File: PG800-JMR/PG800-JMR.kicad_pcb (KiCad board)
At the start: 2 copper layers, 93.5 x 124.5 mm, 51 parts, among them J1 DIN-6, J10 POT_POWER_2, J11 POT_POWER_3, J2 POT_CENTERS_1, J3 POT_CENTERS_2, J4 POT_CENTERS_3, J5 SWITCH_BLK, J6 TEENSY_PIN_BLK1, J7 TEENSY_PIN_BLK3, J8 TEENSY_PIN_BLK2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

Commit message: updated kicad drawings, tweaked code slightly
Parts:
- added J12: GND_BLK, Connector_PinHeader_2.54mm:PinHeader_1x09_P2.54mm_Vertical, F.Cu at (21.9, 112.5)
- added J13: 3.3V_BLK, Connector_PinHeader_2.54mm:PinHeader_1x09_P2.54mm_Vertical, F.Cu at (17.8, 86.5)
- added J14: 5V_BLK, Connector_PinHeader_2.54mm:PinHeader_1x09_P2.54mm_Vertical, F.Cu at (21.7, 86.5)
- moved C7 3.09 mm to (15.7, 120.0)
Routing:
- net +5V: track 107.8 -> 137.4 mm
- net Net-(U3-~{E}): track 133.8 -> 139.0 mm
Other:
- board text added: "JMR-800 JX8P Controller v.0.2 April 2025"
- board text removed: "JMR-800 JX8P Controller v.0.2 March 2026"

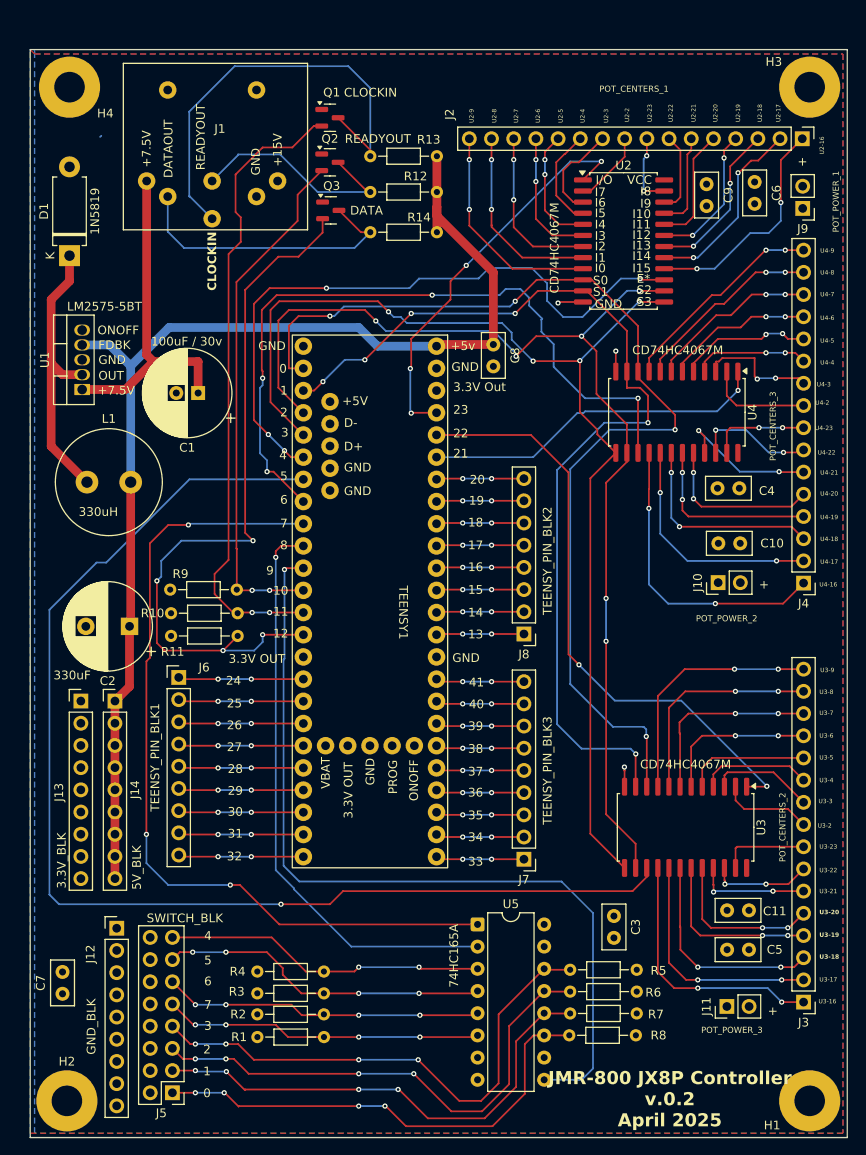
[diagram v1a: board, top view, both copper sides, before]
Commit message: updated PCB design, added optional 3.3V regulator, added another mux
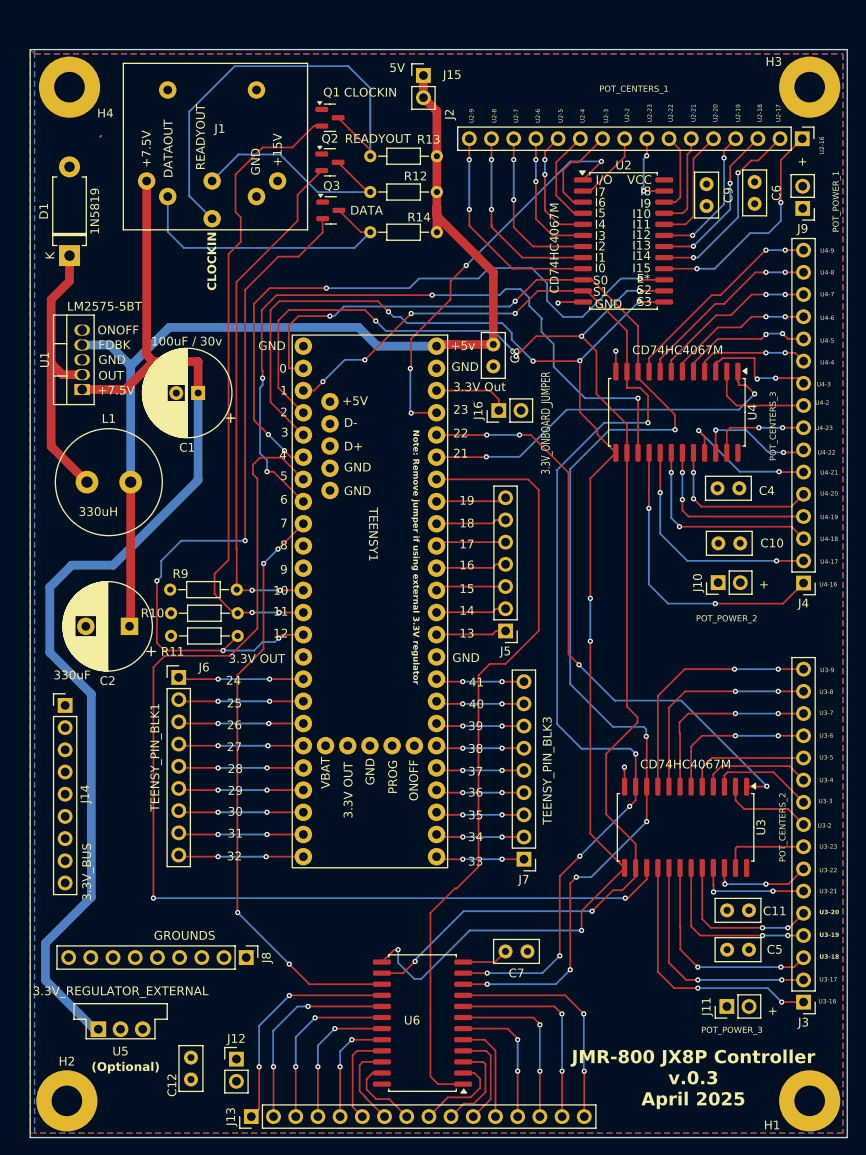
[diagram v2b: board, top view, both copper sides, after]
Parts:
- removed C3: 0.1uF, Capacitor_THT:C_Disc_D5.0mm_W2.5mm_P2.50mm
- removed R1, R2, R3, R4, R5, R6, R7, R8: 5k, Resistor_THT:R_Axial_DIN0204_L3.6mm_D1.6mm_P7.62mm_Horizontal
- added C12: 0.1uF, Capacitor_THT:C_Disc_D5.0mm_W2.5mm_P2.50mm, F.Cu at (30.4, 129.8)
- added J15: 5V, Connector_PinHeader_2.54mm:PinHeader_1x02_P2.54mm_Vertical, F.Cu at (57.0, 15.0)
- added J16: 3.3V_ONBOARD_JUMPER, Connector_PinHeader_2.54mm:PinHeader_1x02_P2.54mm_Vertical, F.Cu at (65.6, 53.3)
- added U6: CD74HC4067M, Package_SO:SOIC-24W_7.5x15.4mm_P1.27mm, F.Cu at (56.9, 123.4)
- J12: value GND_BLK -> POT_POWER_4; footprint Connector_PinHeader_2.54mm:PinHeader_1x09_P2.54mm_Vertical -> Connector_PinHeader_2.54mm:PinHeader_1x02_P2.54mm_Vertical
- J13: value 3.3V_BLK -> POT_CENTERS_4; footprint Connector_PinHeader_2.54mm:PinHeader_1x09_P2.54mm_Vertical -> Connector_PinHeader_2.54mm:PinHeader_1x16_P2.54mm_Vertical
- J14: value 5V_BLK -> 3.3V_BUS
- J5: value SWITCH_BLK -> TEENSY_PIN_BLK2; footprint Connector_PinHeader_2.54mm:PinHeader_2x08_P2.54mm_Vertical -> Connector_PinHeader_2.54mm:PinHeader_1x07_P2.54mm_Vertical
- J8: value TEENSY_PIN_BLK2 -> GROUNDS; footprint Connector_PinHeader_2.54mm:PinHeader_1x08_P2.54mm_Vertical -> Connector_PinHeader_2.54mm:PinHeader_1x09_P2.54mm_Vertical
- U5: value 74HC165A -> 3.3V_REGULATOR_EXTERNAL; footprint Package_DIP:DIP-16_W7.62mm -> Converter_DCDC:Converter_DCDC_Murata_OKI-78SR_Vertical
- moved J5 65.2 mm to (66.4, 78.5)
- moved C7 53.4 mm to (68.9, 115.2), turned to 180 degrees
- moved J13 51.4 mm to (37.3, 134.1), turned to 90 degrees
- moved J8 48.8 mm to (36.7, 115.9), turned to -90 degrees
- moved U5 45.0 mm to (19.8, 124.1)
- moved J12 20.3 mm to (35.6, 127.5)
- moved J14 5.72 mm to (16.0, 87.0)
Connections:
- net Net-(U2-S0) renamed /S0
- net Net-(U2-S1) renamed /S1
- net Net-(U2-S2) renamed /S2
- net Net-(U2-S3) renamed /S3
- J12 pad 2: GND -> /3.3V
- J13 pad 1: /3.3V -> Net-(J13-Pin_1)
- J13 pad 2: /3.3V -> Net-(J13-Pin_2)
- J13 pad 3: /3.3V -> Net-(J13-Pin_3)
- J13 pad 4: /3.3V -> Net-(J13-Pin_4)
- J13 pad 5: /3.3V -> Net-(J13-Pin_5)
- J13 pad 6: /3.3V -> Net-(J13-Pin_6)
- J13 pad 7: /3.3V -> Net-(J13-Pin_7)
- J13 pad 8: /3.3V -> Net-(J13-Pin_8)
- J13 pad 9: /3.3V -> Net-(J13-Pin_9)
- J14 pad 1: +5V -> /3.3V
- J14 pad 2: +5V -> /3.3V
- J14 pad 3: +5V -> /3.3V
- J14 pad 4: +5V -> /3.3V
- J14 pad 5: +5V -> /3.3V
- J14 pad 6: +5V -> /3.3V
- J14 pad 7: +5V -> /3.3V
- J14 pad 8: +5V -> /3.3V
- J14 pad 9: +5V -> /3.3V
- J5 pad 2: /3.3V -> Net-(J5-Pin_2)
- J5 pad 4: /3.3V -> Net-(J5-Pin_4)
- J5 pad 6: /3.3V -> Net-(J5-Pin_6)
- J8 pad 1: Net-(J8-Pin_1) -> GND
- J8 pad 2: Net-(J8-Pin_2) -> GND
- J8 pad 3: Net-(J8-Pin_3) -> GND
- J8 pad 4: Net-(J8-Pin_4) -> GND
- J8 pad 5: Net-(J8-Pin_5) -> GND
- J8 pad 6: Net-(J8-Pin_6) -> GND
- J8 pad 7: Net-(J8-Pin_7) -> GND
- J8 pad 8: Net-(J8-Pin_8) -> GND
- TEENSY1 pad 13: Net-(J8-Pin_1) -> Net-(J5-Pin_1)
- TEENSY1 pad 14: Net-(J8-Pin_2) -> Net-(J5-Pin_2)
- TEENSY1 pad 15: Net-(J8-Pin_3) -> Net-(J5-Pin_3)
- TEENSY1 pad 16: Net-(J8-Pin_4) -> Net-(J5-Pin_4)
- TEENSY1 pad 17: Net-(J8-Pin_5) -> Net-(J5-Pin_5)
- TEENSY1 pad 18: Net-(J8-Pin_6) -> Net-(J5-Pin_6)
- TEENSY1 pad 19: Net-(J8-Pin_7) -> Net-(J5-Pin_7)
- TEENSY1 pad 20: Net-(J8-Pin_8) -> Net-(U6-COM)
- TEENSY1 pad 3.3VOUT: /3.3V -> Net-(J16-Pin_1)
- TEENSY1 pad 7: Net-(U5-~{PL}) -> Net-(U6-~{E})
- TEENSY1 pad 8: Net-(U5-CP) -> unconnected-(TEENSY1-Pad8)
- TEENSY1 pad 9: Net-(U5-Q7) -> unconnected-(TEENSY1-Pad9)
- U5 pad 1: Net-(U5-~{PL}) -> +7.5V
- U5 pad 2: Net-(U5-CP) -> GND
- U5 pad 3: Net-(J5-Pin_15) -> /3.3V
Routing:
- net Net-(U5-Q7): track 97.7 -> 0.00 mm, vias 1 -> 0
- net Net-(U5-~{PL}): track 96.1 -> 0.00 mm, vias 3 -> 0
- net Net-(U6-COM): track 0.00 -> 89.7 mm
- net +7.5V: track 39.2 -> 128.7 mm
- net Net-(U6-~{E}): track 0.00 -> 67.5 mm, vias 0 -> 4
- net Net-(U5-CP): track 66.7 -> 0.00 mm, vias 1 -> 0
- net Net-(J5-Pin_7): track 60.0 -> 8.08 mm, vias 4 -> 0
- net Net-(J5-Pin_5): track 58.1 -> 8.08 mm, vias 4 -> 0
- net Net-(J5-Pin_3): track 55.8 -> 8.08 mm, vias 4 -> 0
- net Net-(J5-Pin_1): track 54.7 -> 8.08 mm, vias 4 -> 0
- net /S0: track 120.4 -> 158.9 mm, vias 4 -> 8
- net Net-(J5-Pin_13): track 37.8 -> 0.00 mm, vias 4 -> 0
- net /S3: track 130.1 -> 167.3 mm, vias 4 -> 8
- net Net-(J5-Pin_15): track 36.8 -> 0.00 mm, vias 2 -> 0
- net Net-(J5-Pin_11): track 36.6 -> 0.00 mm, vias 4 -> 0
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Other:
- board text added: "(Optional)"
- board text added: "JMR-800 JX8P Controller v.0.3 April 2025"
- board text added: "Note: Remove jumper if using external 3.3V regulator"
- board text removed: "20"
- board text removed: "JMR-800 JX8P Controller v.0.2 April 2025"

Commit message: updated readme
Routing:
- net /DATAOUT3.3V: track 82.3 -> 68.7 mm, vias 4 -> 3
- net Net-(U4-COM): track 43.2 -> 40.2 mm
- net /S2: track 163.0 -> 162.0 mm
- net Net-(U3-~{E}): track 124.9 -> 125.5 mm
- net Net-(U2-~{E}): vias 4 -> 2
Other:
- board text added: "20"

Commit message: updated 3d image
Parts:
- added C13: 0.1uF, Capacitor_THT:C_Disc_D5.0mm_W2.5mm_P2.50mm, F.Cu at (22.8, 130.2)
- added J17: LED_REG_CONN, Connector_PinHeader_2.54mm:PinHeader_1x08_P2.54mm_Vertical, F.Cu at (21.8, 97.4)
- added R1: 220, Resistor_THT:R_Axial_DIN0204_L3.6mm_D1.6mm_P2.54mm_Vertical, F.Cu at (27.2, 115.2)
- added R15: 720, Resistor_THT:R_Axial_DIN0204_L3.6mm_D1.6mm_P2.54mm_Vertical, F.Cu at (28.0, 38.2)
- added R2: 220, Resistor_THT:R_Axial_DIN0204_L3.6mm_D1.6mm_P2.54mm_Vertical, F.Cu at (27.2, 112.8)
- added R3: 220, Resistor_THT:R_Axial_DIN0204_L3.6mm_D1.6mm_P2.54mm_Vertical, F.Cu at (27.2, 110.2)
- added R4: 220, Resistor_THT:R_Axial_DIN0204_L3.6mm_D1.6mm_P2.54mm_Vertical, F.Cu at (27.2, 107.5)
- added R5: 220, Resistor_THT:R_Axial_DIN0204_L3.6mm_D1.6mm_P2.54mm_Vertical, F.Cu at (27.2, 105.0)
- added R6: 220, Resistor_THT:R_Axial_DIN0204_L3.6mm_D1.6mm_P2.54mm_Vertical, F.Cu at (27.2, 102.5)
- added R7: 220, Resistor_THT:R_Axial_DIN0204_L3.6mm_D1.6mm_P2.54mm_Vertical, F.Cu at (27.2, 99.8)
- added R8: 220, Resistor_THT:R_Axial_DIN0204_L3.6mm_D1.6mm_P2.54mm_Vertical, F.Cu at (24.0, 93.5)
- added U7: 74HC595, Package_DIP:DIP-16_W7.62mm, F.Cu at (37.2, 122.8)
- J6: footprint Connector_PinHeader_2.54mm:PinHeader_1x09_P2.54mm_Vertical -> Connector_PinHeader_2.54mm:PinHeader_1x06_P2.54mm_Vertical
- moved J8 64.5 mm to (100.4, 126.5)
- moved J2 9.14 mm to (95.0, 14.8)
- moved J15 4.51 mm to (52.5, 14.7)
- moved U5 4.36 mm to (15.5, 123.8)
- moved J5 2.10 mm to (68.5, 78.5)
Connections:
- C4 pad 1: GND -> /3.3V
- C4 pad 2: /3.3V -> GND
- TEENSY1 pad 30: Net-(J6-Pin_7) -> Net-(U7-RCLK)
- TEENSY1 pad 31: Net-(J6-Pin_8) -> Net-(U7-SRCLK)
- TEENSY1 pad 32: Net-(J6-Pin_9) -> Net-(U7-SER)
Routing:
- net Net-(U7-SRCLK): track 0.00 -> 43.8 mm, vias 0 -> 1
- net Net-(U7-QC): track 0.00 -> 40.4 mm, vias 0 -> 2
- net Net-(U7-SER): track 0.00 -> 28.4 mm, vias 0 -> 5
- net Net-(U7-RCLK): track 0.00 -> 24.3 mm, vias 0 -> 5
- net Net-(U7-QB): track 0.00 -> 23.6 mm, vias 0 -> 2
- net Net-(U7-QH): track 0.00 -> 21.3 mm
- net Net-(U3-~{E}): track 125.5 -> 105.7 mm, vias 2 -> 4
- net Net-(U7-QD): track 0.00 -> 18.2 mm
- net Net-(U7-QF): track 0.00 -> 16.3 mm
- net Net-(U7-QG): track 0.00 -> 15.9 mm
- net Net-(U7-QE): track 0.00 -> 15.8 mm, vias 0 -> 1
- net Net-(J6-Pin_9): track 14.3 -> 0.00 mm, vias 2 -> 0
- net Net-(J6-Pin_8): track 14.3 -> 0.00 mm, vias 2 -> 0
- net Net-(J6-Pin_7): track 14.3 -> 0.00 mm, vias 2 -> 0
- net Net-(J2-Pin_13): track 15.3 -> 25.0 mm
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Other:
- board text added: "JMR800 JX8P Controller v.0.3 April 2025"
- board text removed: "(Optional)"
- board text removed: "JMR-800 JX8P Controller v.0.3 April 2025"

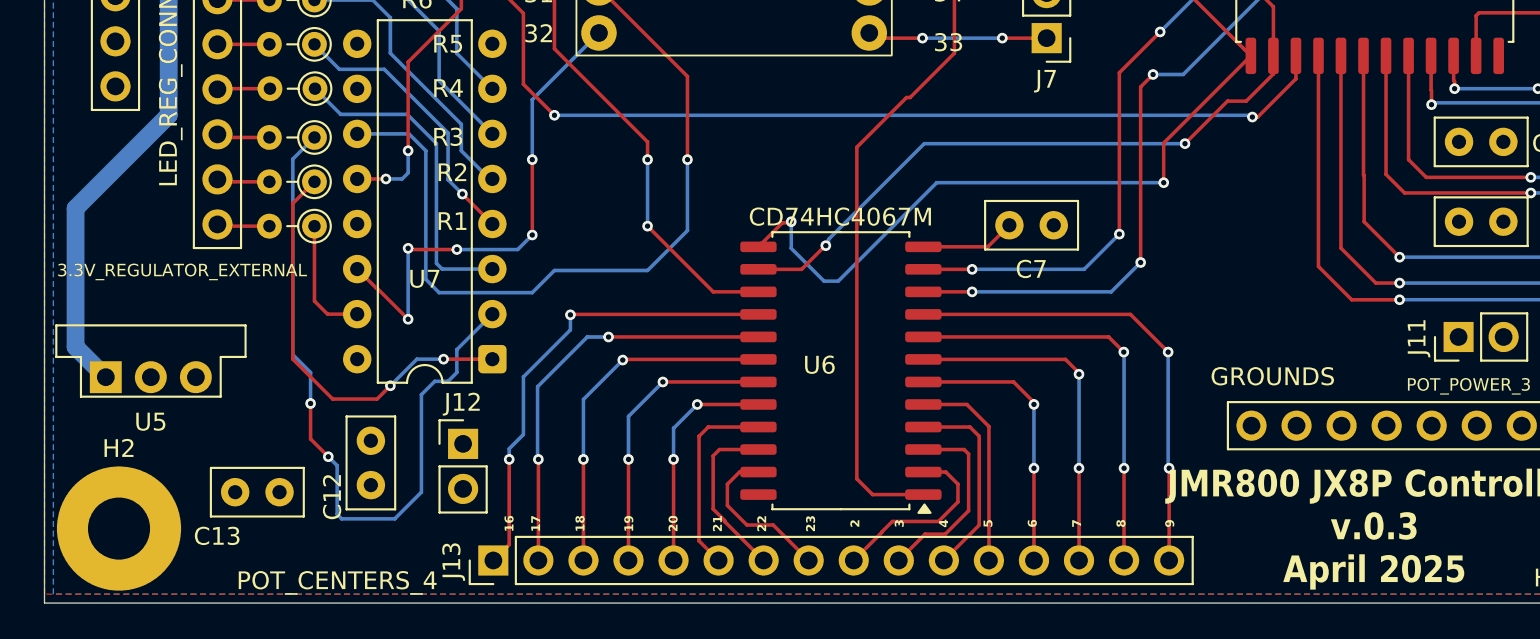
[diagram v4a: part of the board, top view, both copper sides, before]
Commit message: Fixed LM1117-3.3, pins in wrong order
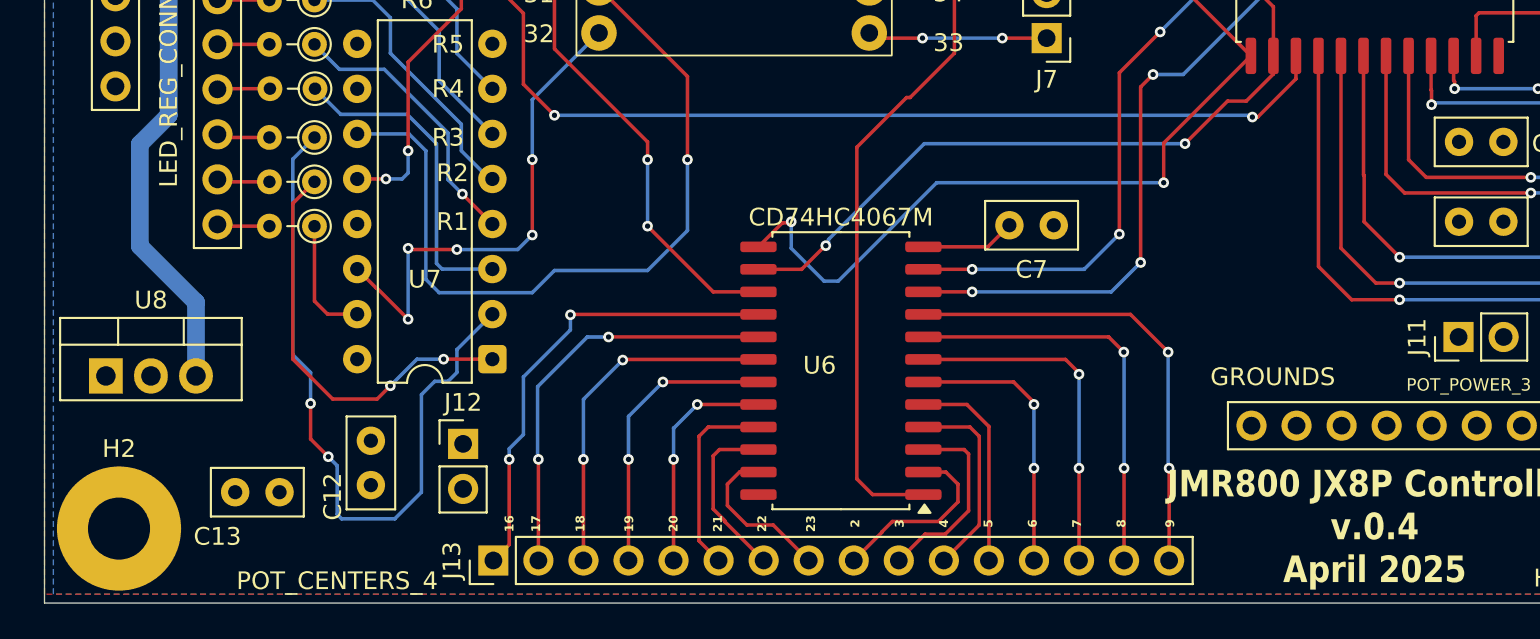
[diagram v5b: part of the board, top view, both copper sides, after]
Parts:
- removed U5: 3.3V_REGULATOR_EXTERNAL, Converter_DCDC:Converter_DCDC_Murata_OKI-78SR_Vertical
- added U8: LM1117T-3.3, Package_TO_SOT_THT:TO-220-3_Vertical, F.Cu at (15.5, 123.7)
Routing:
- net +7.5V: track 126.3 -> 125.3 mm
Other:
- board text added: "JMR800 JX8P Controller v.0.4 April 2025"
- board text removed: "JMR800 JX8P Controller v.0.3 April 2025"
